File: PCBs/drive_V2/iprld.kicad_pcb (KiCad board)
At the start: 2 copper layers, 100 x 100 mm, 83 parts, among them IC1 W25Q16JVUXIQ_TR, IC2 ADS1115IDGSR, J12 TYPE-C-31-M-12, U1 AMS1117-3.3, U11 4N35, U12 4N35, U13 4N35, U14 4N35, U2 ESP32-S3, U3 4N35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

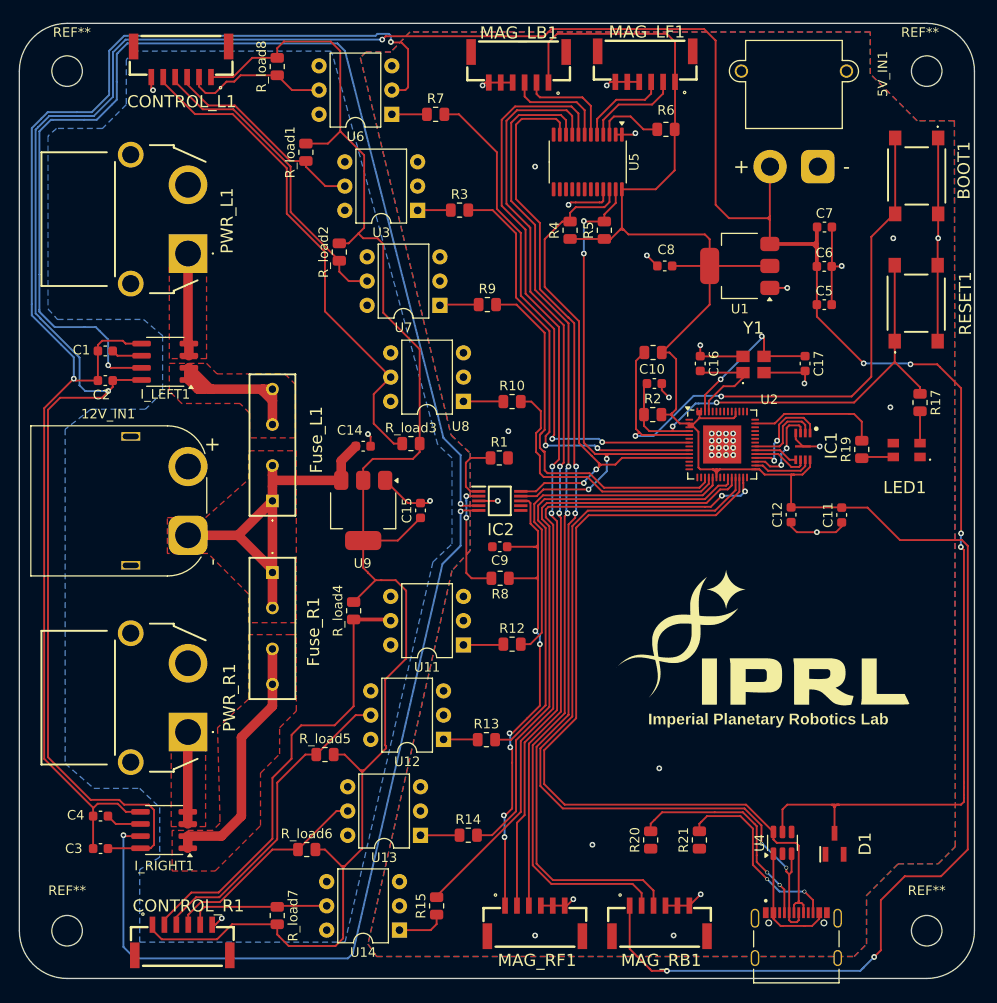
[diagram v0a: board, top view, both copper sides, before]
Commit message: Fixed some DRC errors
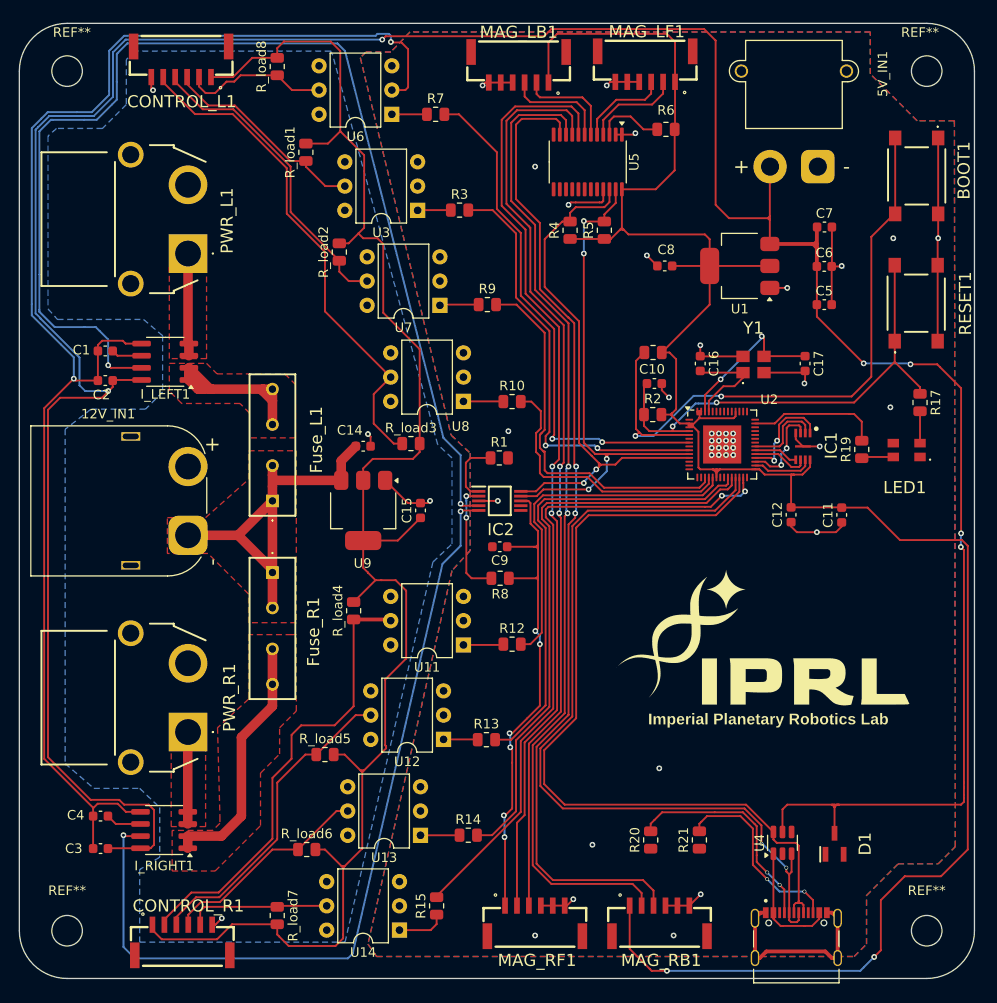
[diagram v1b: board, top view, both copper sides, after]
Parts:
- removed J12: TYPE-C-31-M-12, main_lib:TYPE-C-31-M-12
- added J1: TYPE-C-31-M-12, iprl_footprints:TYPE-C-31-M-12, F.Cu at (81.3, 97.9)
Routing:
- net GND: track 231.8 -> 252.1 mm

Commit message: Found some issues in the drive schematic and PCB
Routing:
- net +3.3V: track 279.1 -> 300.0 mm
- net /VBUS: track 12.9 -> 19.3 mm
- net GND: track 252.1 -> 254.3 mm, vias 42 -> 43
- net /+12V_R: track 9.64 -> 8.37 mm
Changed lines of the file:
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@@
 			(at 0.5 -4.05 0)
 			(layer "F.SilkS")
+			(hide yes)
 			(effects
 				(font
@@
 			(at 0 -4.2 0)
 			(layer "F.SilkS")
+			(hide yes)
 			(effects
 				(font
@@
 			(at 0 -4.2 0)
 			(layer "F.SilkS")
+			(hide yes)
 			(effects
 				(font
@@
 			(at -0.7 -4.05 0)
 			(layer "F.SilkS")
+			(hide yes)
 			(effects
 				(font
@@
 	)
 	(segment
+		(start 79.6 87.2375)
+		(end 79.6 89.1)
+		(width 0.2)
+		(layer "F.Cu")
+		(net 1)
+	)
+	(segment
 		(start 57.75 18.75)
 		(end 57.5 19)
@@
 	)
 	(segment
+		(start 79.9 86.9375)
+		(end 79.6 87.2375)
+		(width 0.2)
+		(layer "F.Cu")
+		(net 1)
+	)
+	(segment
 		(start 8.2 81.7)
 		(end 7.725 82.175)
@@
 	)
 	(via
+		(at 79.6 89.1)
+		(size 0.4)
+		(drill 0.3)
+		(layers "F.Cu" "B.Cu")
+		(net 1)
+	)
+	(via
 		(at 74.7375 43.69375)
 		(size 0.6)
@@
 	)
 	(segment
+		(start 50.85 97.15)
+		(end 50.85 92.373885)
+		(width 0.2)
+		(layer "F.Cu")
+		(net 5)
+	)
+	(segment
 		(start 92.7 89.3)
 		(end 96.5 89.3)
@@
 	)
 	(segment
+		(start 52.9 99.2)
+		(end 50.85 97.15)
+		(width 0.2)
+		(layer "F.Cu")
+		(net 5)
+	)
+	(segment
 		(start 54.1 58.1)
 		(end 54.3 57.9)
@@
 	)
 	(segment
+		(start 66.2 99.2)
+		(end 52.9 99.2)
+		(width 0.2)
+		(layer "F.Cu")
+		(net 5)
+	)
+	(segment
 		(start 68.6125 15.3875)
 		(end 68.6125 11.1)
@@
 	)
 	(segment
+		(start 84.4 88.7)
+		(end 83.75 89.35)
+		(width 0.2)
+		(layer "F.Cu")
+		(net 12)
+	)
+	(segment
+		(start 84.4 87)
+		(end 84.4 88.7)
+		(width 0.2)
+		(layer "F.Cu")
+		(net 12)
+	)
+	(segment
 		(start 83.75 93.1125)
 		(end 83.75 93.75)
@@
 	)
 	(segment
+		(start 83.75 89.35)
+		(end 83.75 93.1125)
+		(width 0.2)
+		(layer "F.Cu")
+		(net 12)
+	)
+	(segment
 		(start 78.95 93.1125)
 		(end 78.95 86.9375)
@@
 		(width 1)
 		(layer "F.Cu")
-		(net 29)
-	)
-	(segment
-		(start 17.635 83.825)
-		(end 17.635 82.555)
-		(width 1)
-		(layer "F.Cu")
